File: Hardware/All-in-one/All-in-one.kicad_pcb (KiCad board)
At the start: 2 copper layers, 1 part, among them U1 DHT11

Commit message: Схема электрическая принципиальная All-in-one/
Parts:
- added J1: Conn_01x04_Male, Connector_PinHeader_2.54mm:PinHeader_1x04_P2.54mm_Vertical, F.Cu at (143.9, 128.3)
- added J2: Barrel_Jack, Connector_BarrelJack:BarrelJack_Horizontal, F.Cu at (175.5, 133.6)
- added J4: Conn_01x02_Male, Connector_PinHeader_2.54mm:PinHeader_1x02_P2.54mm_Vertical, F.Cu at (143.5, 138.5)
- added J5: Conn_01x02_Male, Connector_PinHeader_2.54mm:PinHeader_1x02_P2.54mm_Vertical, F.Cu at (139.3, 138.5)
- added J6: Conn_01x02_Male, Connector_PinHeader_2.54mm:PinHeader_1x02_P2.54mm_Vertical, F.Cu at (172.0, 102.5)
- added J7: Conn_01x02_Male, Connector_PinHeader_2.54mm:PinHeader_1x02_P2.54mm_Vertical, F.Cu at (184.6, 129.0)
- added J8: Conn_01x02_Male, Connector_PinHeader_2.54mm:PinHeader_1x02_P2.54mm_Vertical, F.Cu at (187.2, 125.0)
- added R1: R, Resistor_THT:R_Axial_DIN0207_L6.3mm_D2.5mm_P7.62mm_Horizontal, F.Cu at (171.0, 128.8)
- added R2: R, Resistor_THT:R_Axial_DIN0207_L6.3mm_D2.5mm_P7.62mm_Horizontal, F.Cu at (170.9, 124.9)
- added RTC1: RTC_DS3231, megasaturnv_custom_components:RTC_DS3231, F.Cu at (141.9, 90.5)
- added U2: BMP280_flipped, megasaturnv_custom_components:BMP280_flipped, F.Cu at (135.5, 131.8)
- added U3: YAAJ_BluePill_Part_Like_SWD_Breakout, Footprints:YAAJ_BluePill_SWD_1, F.Cu at (149.8, 92.8)
- added U4: microSD_flipped, megasaturnv_custom_components:microSD_Card_3V3, F.Cu at (171.6, 107.4)
- moved U1 17.0 mm to (113.7, 93.0)

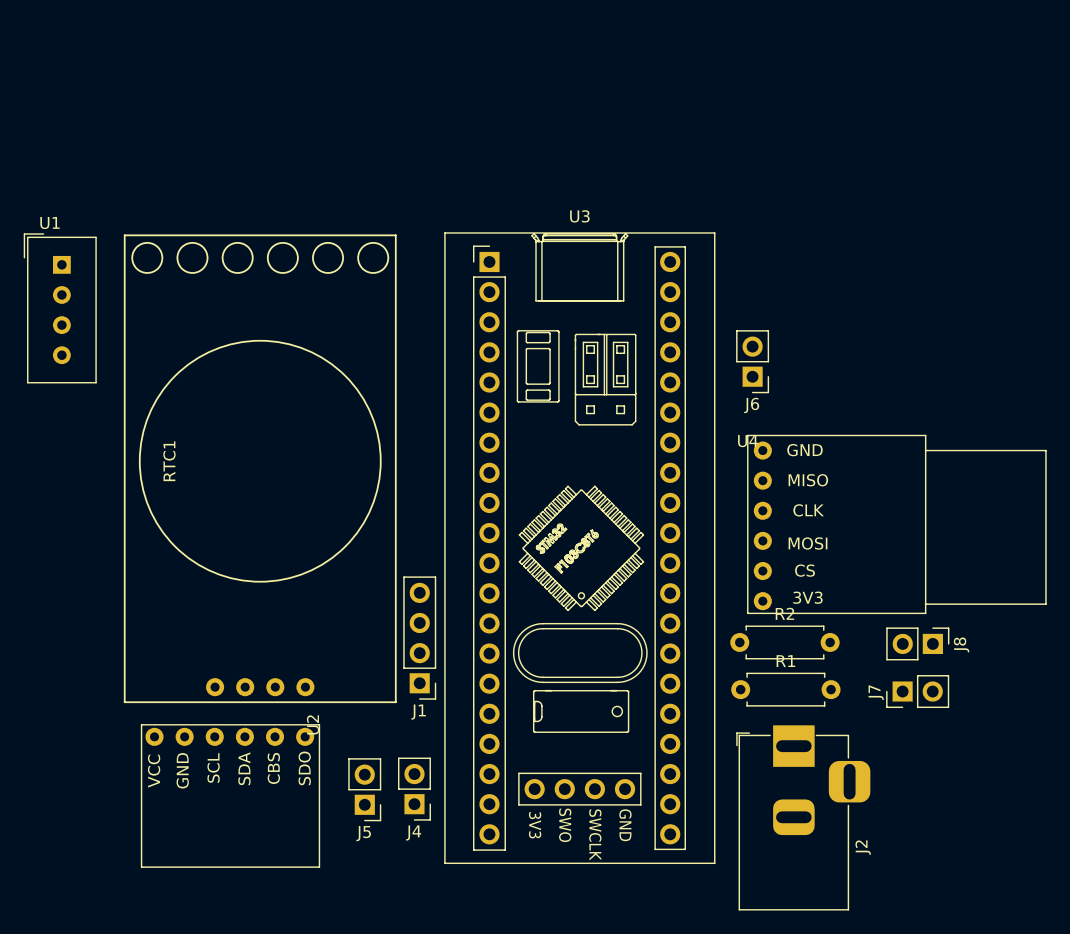
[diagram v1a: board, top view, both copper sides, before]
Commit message: Продолжаем разводить п.п. На морозе часы неожиданно сбросились. справлени баг со слишком ранним выходом из режима настройки часов. 30 секунд недостаточно, чтобы точно сбросить секунды
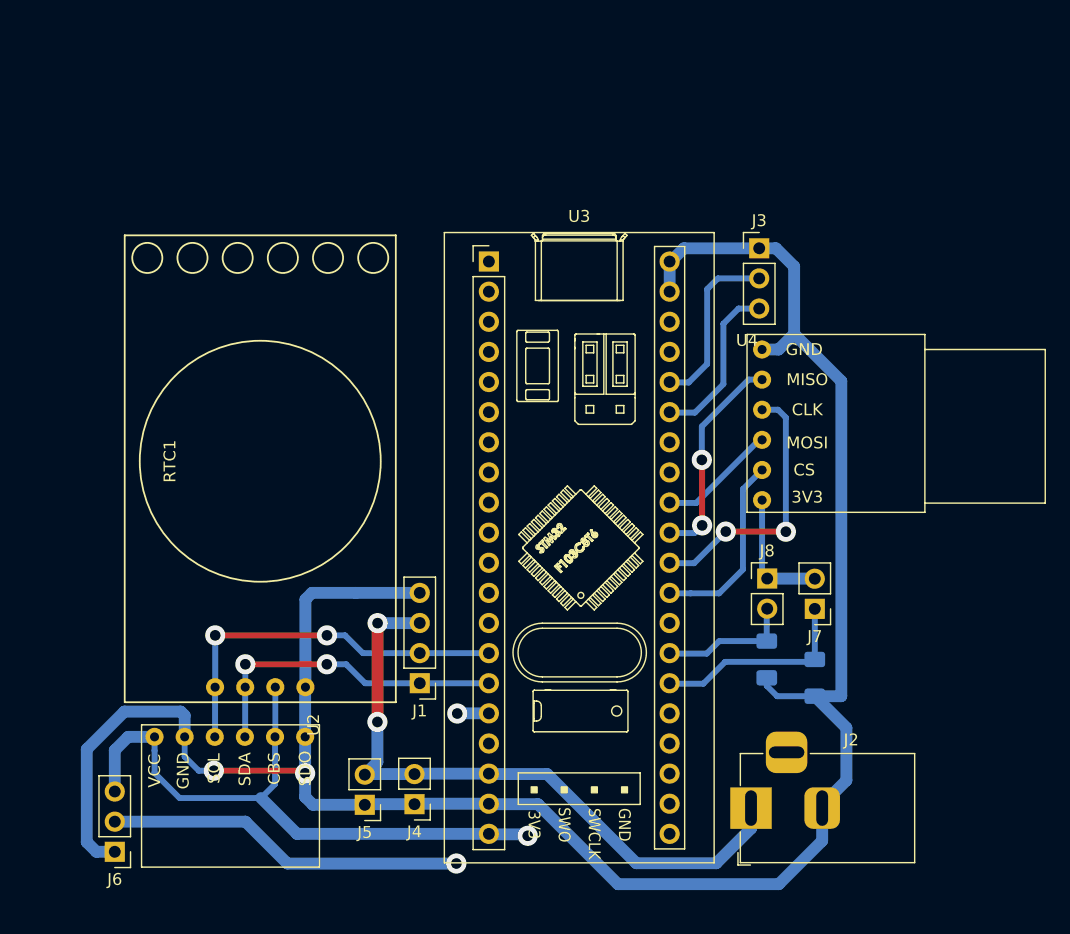
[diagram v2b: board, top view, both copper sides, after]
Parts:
- removed U1: DHT11, Sensor:Aosong_DHT11_5.5x12.0_P2.54mm
- added J3: Conn_01x03, Connector_PinHeader_2.54mm:PinHeader_1x03_P2.54mm_Vertical, F.Cu at (172.5, 91.6)
- J6: value Conn_01x02_Male -> Conn_01x03; footprint Connector_PinHeader_2.54mm:PinHeader_1x02_P2.54mm_Vertical -> Connector_PinHeader_2.54mm:PinHeader_1x03_P2.54mm_Vertical
- R1, R2: value R -> 10k; footprint Resistor_THT:R_Axial_DIN0207_L6.3mm_D2.5mm_P7.62mm_Horizontal -> Resistor_SMD:R_1206_3216Metric_Pad1.30x1.75mm_HandSolder; moved to B.Cu
- U3: value YAAJ_BluePill_Part_Like_SWD_Breakout -> YAAJ_BluePill_Part_Like; footprint Footprints:YAAJ_BluePill_SWD_1 -> Footprints:YAAJ_BluePill_1
- moved J6 67.1 mm to (118.2, 142.5)
- moved J8 15.0 mm to (173.2, 119.5), turned to 0 degrees
- moved J7 10.2 mm to (177.2, 122.0), turned to 180 degrees
- moved U4 8.52 mm to (171.5, 98.9)
- moved J2 6.35 mm to (171.9, 138.8), turned to 180 degrees
- moved R1 6.33 mm to (177.2, 127.8), turned to 90 degrees
- moved R2 2.69 mm to (173.2, 126.3), turned to 90 degrees
- moved U3 0.06 mm to (149.7, 92.7)
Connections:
- J6 pad 1: Net-(J6-Pad1) -> GND
- J6 pad 2: Net-(J6-Pad2) -> DHT_11
- J7 pad 2: GND -> 3V3
- J8 pad 1: GND -> 3V3
- R1 pad 1: 3V3 -> GND
- R2 pad 1: 3V3 -> GND
- RTC1 pad 2: +5V -> 3V3
- U3 pad 16: Net-(U3-Pad16) -> DHT_11
- U3 pad 35: Net-(J6-Pad1) -> Net-(J3-Pad3)
- U3 pad 36: Net-(J6-Pad2) -> Net-(J3-Pad2)
- U3 pad 38: Net-(U3-Pad38) -> 3V3
- U3 pad 39: Net-(U3-Pad39) -> GND
- U3 pad 40: Net-(U3-Pad40) -> GND
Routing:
- net GND: track 0.00 -> 186.1 mm, vias 0 -> 2
- net 3V3: track 0.00 -> 64.6 mm, vias 0 -> 1
- net +5V: track 0.00 -> 55.4 mm, vias 0 -> 2
- net DHT_11: track 0.00 -> 32.9 mm, vias 0 -> 2
- net I2C1_SCL: track 0.00 -> 32.3 mm, vias 0 -> 2
- net I2C1_SDA: track 0.00 -> 27.3 mm, vias 0 -> 2
- net Net-(U3-Pad30): track 0.00 -> 23.3 mm, vias 0 -> 2
- net Net-(U3-Pad31): track 0.00 -> 18.0 mm, vias 0 -> 2
- net A1: track 0.00 -> 17.3 mm
- net Net-(U3-Pad29): track 0.00 -> 16.0 mm
- net Net-(J3-Pad2): track 0.00 -> 14.8 mm
- net Net-(J3-Pad3): track 0.00 -> 14.1 mm
- net A2: track 0.00 -> 11.3 mm
- net Net-(U3-Pad32): track 0.00 -> 10.4 mm
